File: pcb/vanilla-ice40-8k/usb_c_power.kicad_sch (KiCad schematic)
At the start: 25 parts, among them J5 Conn_01x02_Pin, U5 TPS563252DRLR, U6 TPS563252DRLR

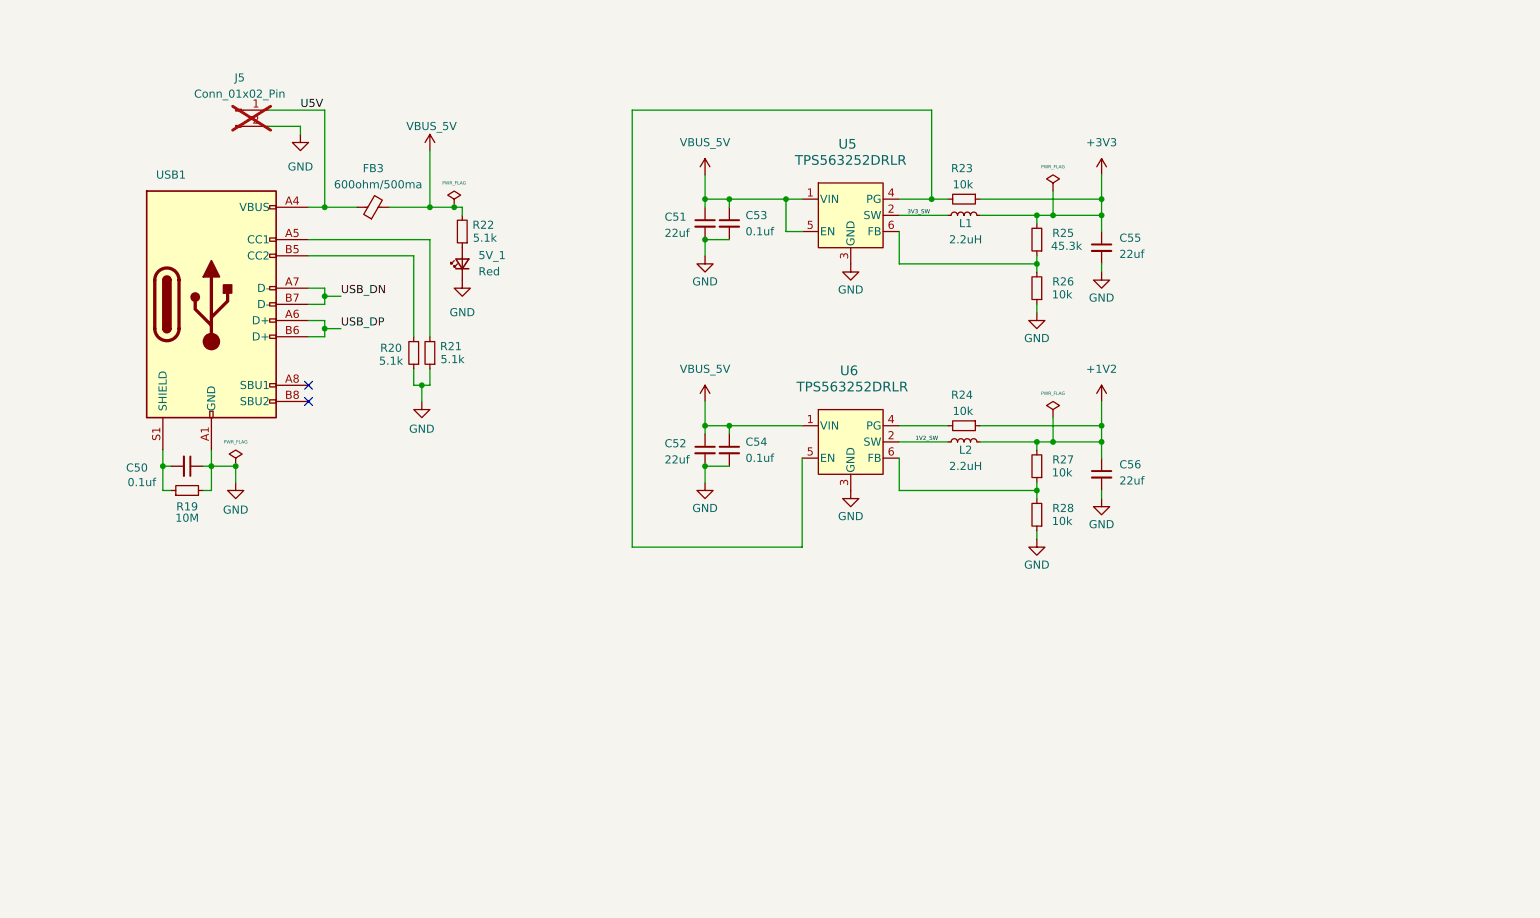
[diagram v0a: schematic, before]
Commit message: [pcb][hx8k] redid components with vip
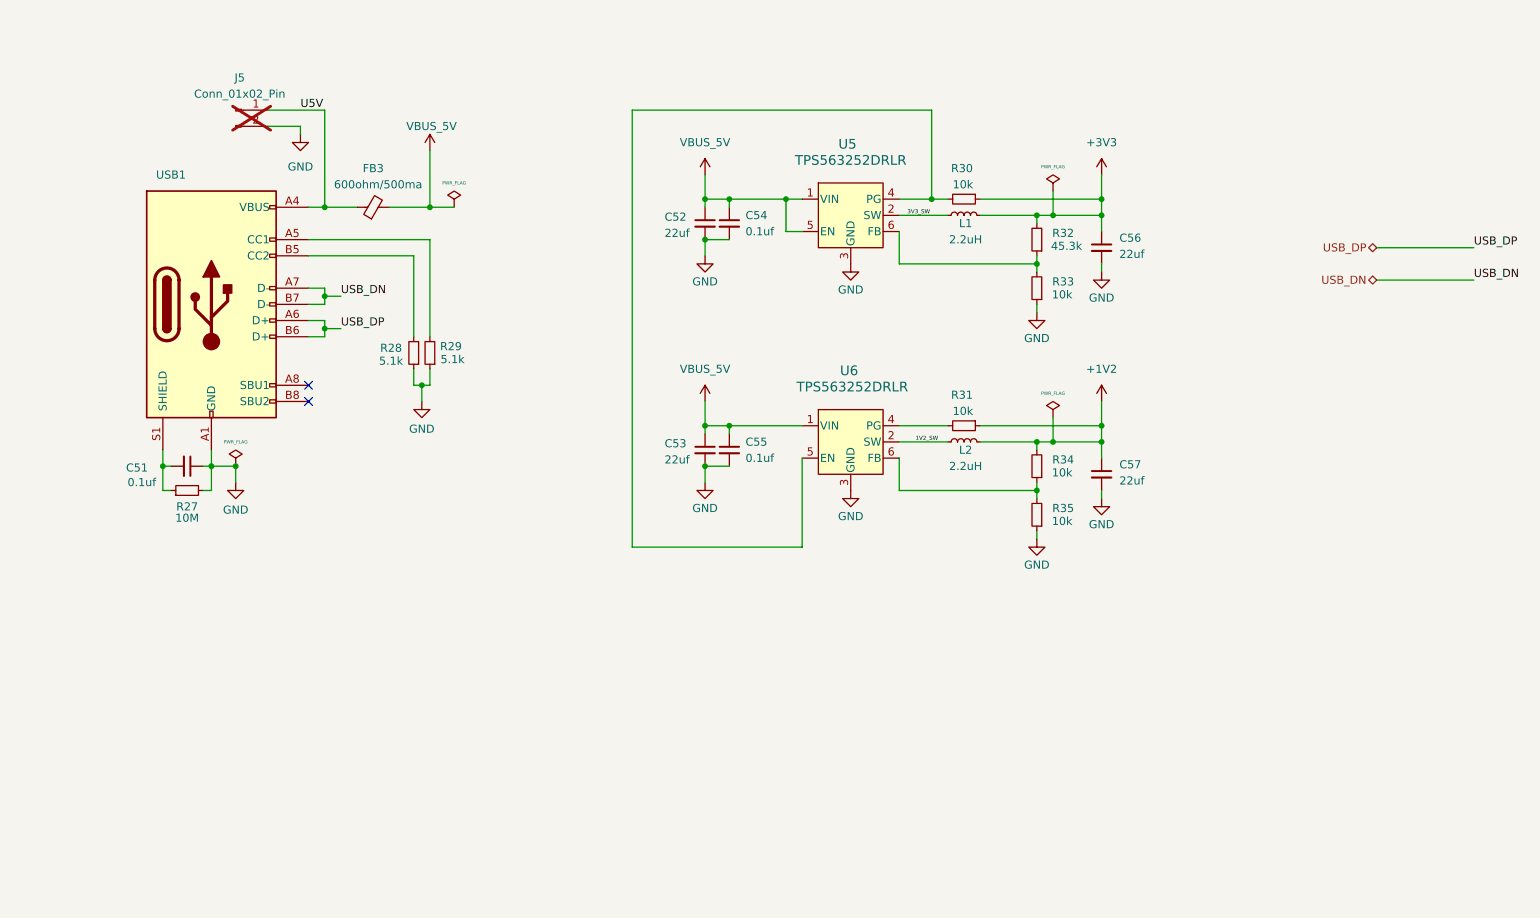
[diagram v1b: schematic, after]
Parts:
- removed 5V_1: Red, Diode_SMD:D_0603_1608Metric, symbol Device:LED_Small
- removed R22: 5.1k, Resistor_SMD:R_0603_1608Metric, symbol Device:R_Small
- renumbered C50 to C51, C51 to C52, C52 to C53, C53 to C54, C54 to C55, C55 to C56, C56 to C57, R19 to R27, R20 to R28, R21 to R29, R23 to R30, R24 to R31, R25 to R32, R26 to R33, R27 to R34, R28 to R35

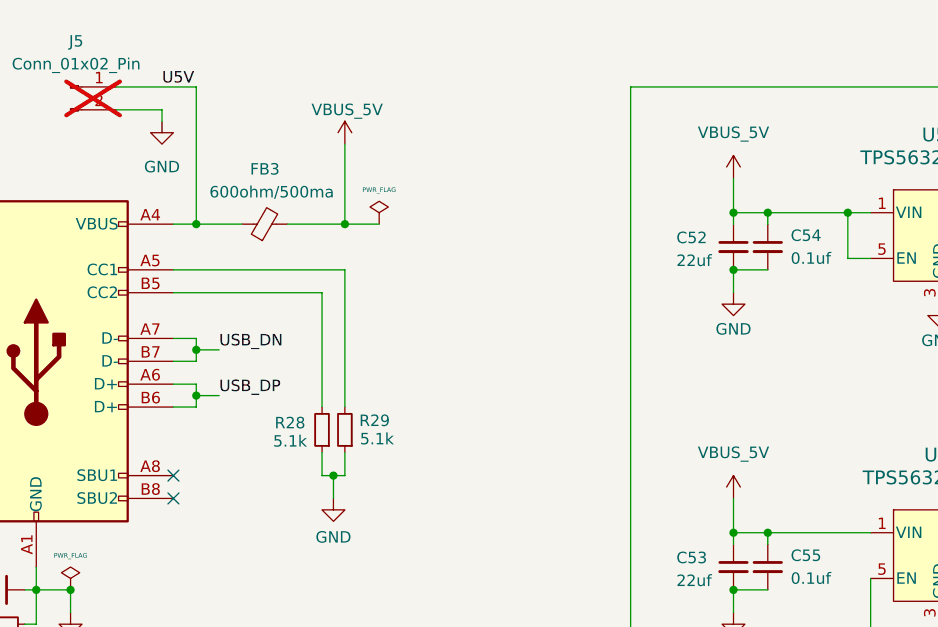
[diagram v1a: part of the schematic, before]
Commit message: [pcb][hx8k] incoming power cleanup
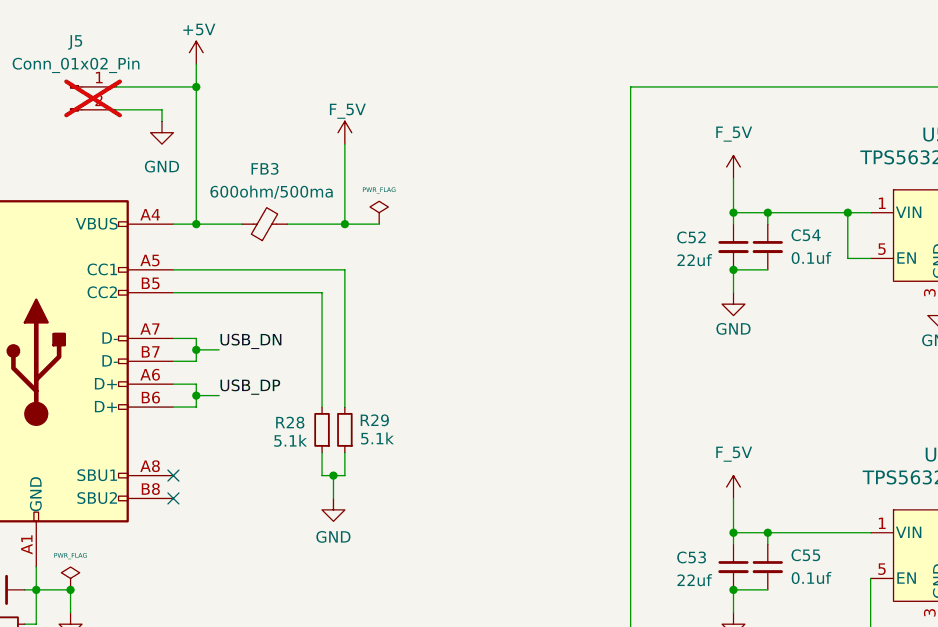
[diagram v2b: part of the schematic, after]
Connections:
- net U5V renamed +5V
- net VBUS_5V renamed F_5V
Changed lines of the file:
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@@
 	)
 	(junction
+		(at 73.66 39.37)
+		(diameter 0)
+		(color 0 0 0 0)
+	)
+	(junction
 		(at 88.9 82.55)
 		(diameter 0)
@@
 	(wire
 		(pts
+			(xy 73.66 36.83) (xy 73.66 39.37)
+		)
+		(stroke
+			(width 0)
+			(type default)
+		)
+	)
+	(wire
+		(pts
 			(xy 133.35 53.34) (xy 133.35 54.61)
 		)
@@
 		)
 	)
-	(label "U5V"
-		(at 69.85 39.37 0)
-		(fields_autoplaced yes)
-		(effects
-			(font
-				(size 1.27 1.27)
-			)
-			(justify left bottom)
-		)
-	)
 	(label "USB_DP"
 		(at 254 60.96 0)
@@
 			)
 		)
-		(property "Value" "VBUS_5V"
+		(property "Value" "F_5V"
 			(at 133.35 80.01 0)
 			(effects
@@
 	)
 	(symbol
+		(lib_id "power:VBUS")
+		(at 73.66 36.83 0)
+		(unit 1)
+		(exclude_from_sim no)
+		(in_bom yes)
+		(on_board yes)
+		(dnp no)
+		(property "Reference" "#PWR078"
+			(at 73.66 40.64 0)
+			(effects
+				(font
+					(size 1.27 1.27)
+				)
+				(hide yes)
+			)
+		)
+		(property "Value" "+5V"
+			(at 73.914 33.02 0)
+			(effects
+				(font
+					(size 1.27 1.27)
+				)
+			)
+		)
+		(property "Footprint" ""
+			(at 73.66 36.83 0)
+			(effects
+				(font
+					(size 1.27 1.27)
+				)
+				(hide yes)
+			)
+		)
+		(property "Datasheet" ""
+			(at 73.66 36.83 0)
+			(effects
+				(font
+					(size 1.27 1.27)
+				)
+				(hide yes)
+			)
+		)
+		(property "Description" "Power symbol creates a global label with name \"VBUS\""
+			(at 73.66 36.83 0)
+			(effects
+				(font
+					(size 1.27 1.27)
+				)
+				(hide yes)
+			)
+		)
+		(pin "1"
+		)
+		(instances
+			(project "vanilla-ice40-8k"
+				(path "/6fdfbf4b-014a-4077-8dc3-7ce5ecaf5fe5/4c09157d-3537-4cf3-bc9c-21379ec730e4"
+					(reference "#PWR078")
+					(unit 1)
+				)
+			)
+		)
+	)
+	(symbol
 		(lib_id "power:GND")
 		(at 195.58 64.77 0)
@@
 			)
 		)
-		(property "Value" "VBUS_5V"
+		(property "Value" "F_5V"
 			(at 133.35 44.45 0)
 			(effects
@@
 			)
 		)
-		(property "Value" "VBUS_5V"
+		(property "Value" "F_5V"
 			(at 90.424 41.91 0)
 			(effects

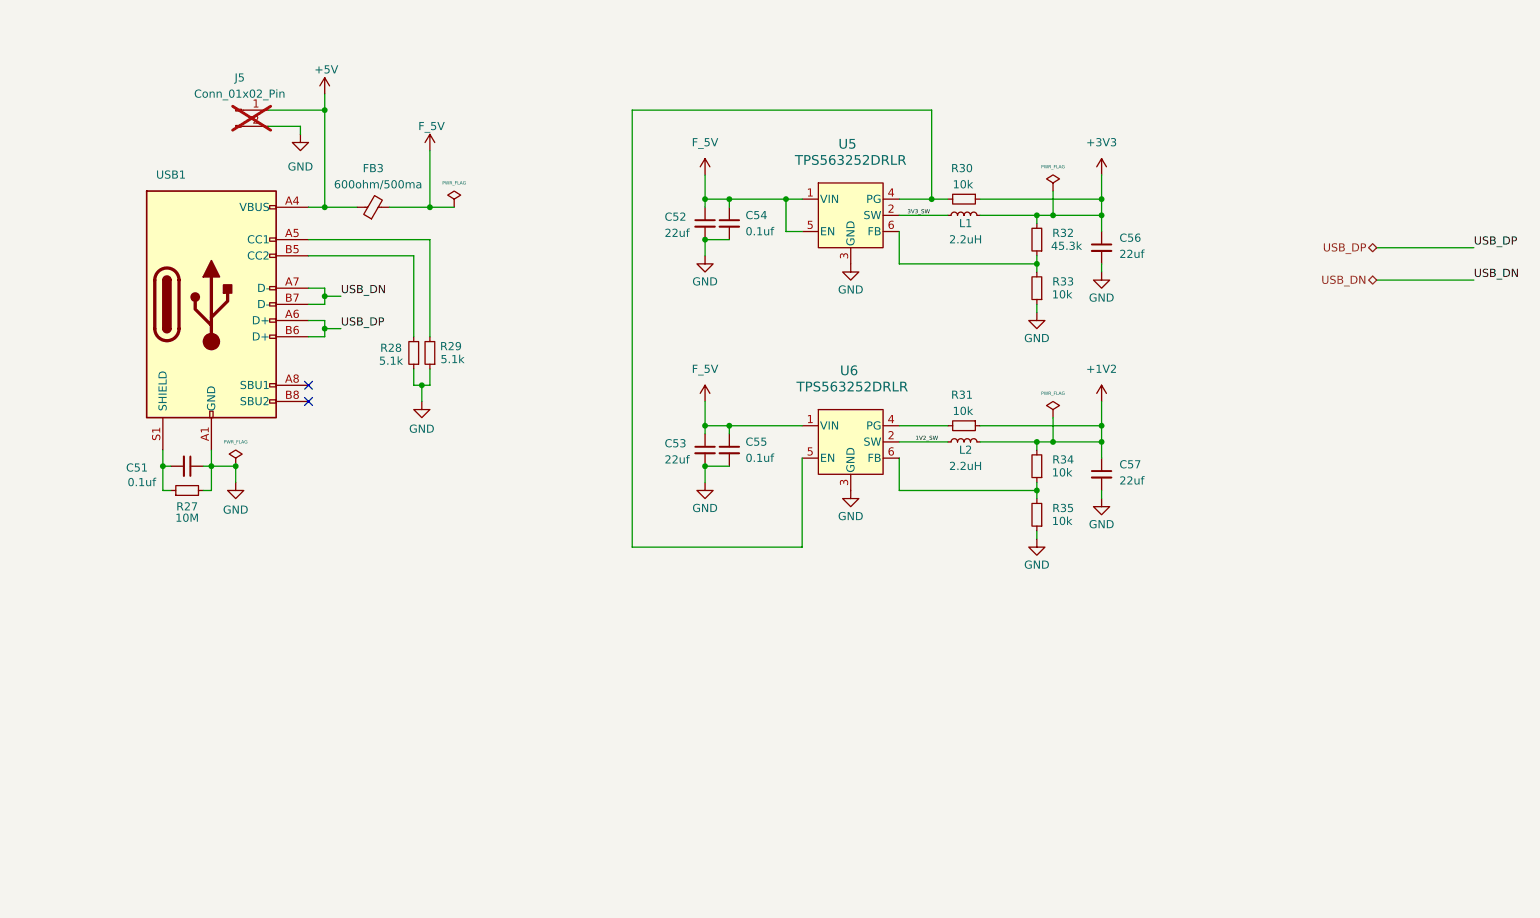
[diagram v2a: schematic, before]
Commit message: [pcb][hx8k] rerouted; all pins done
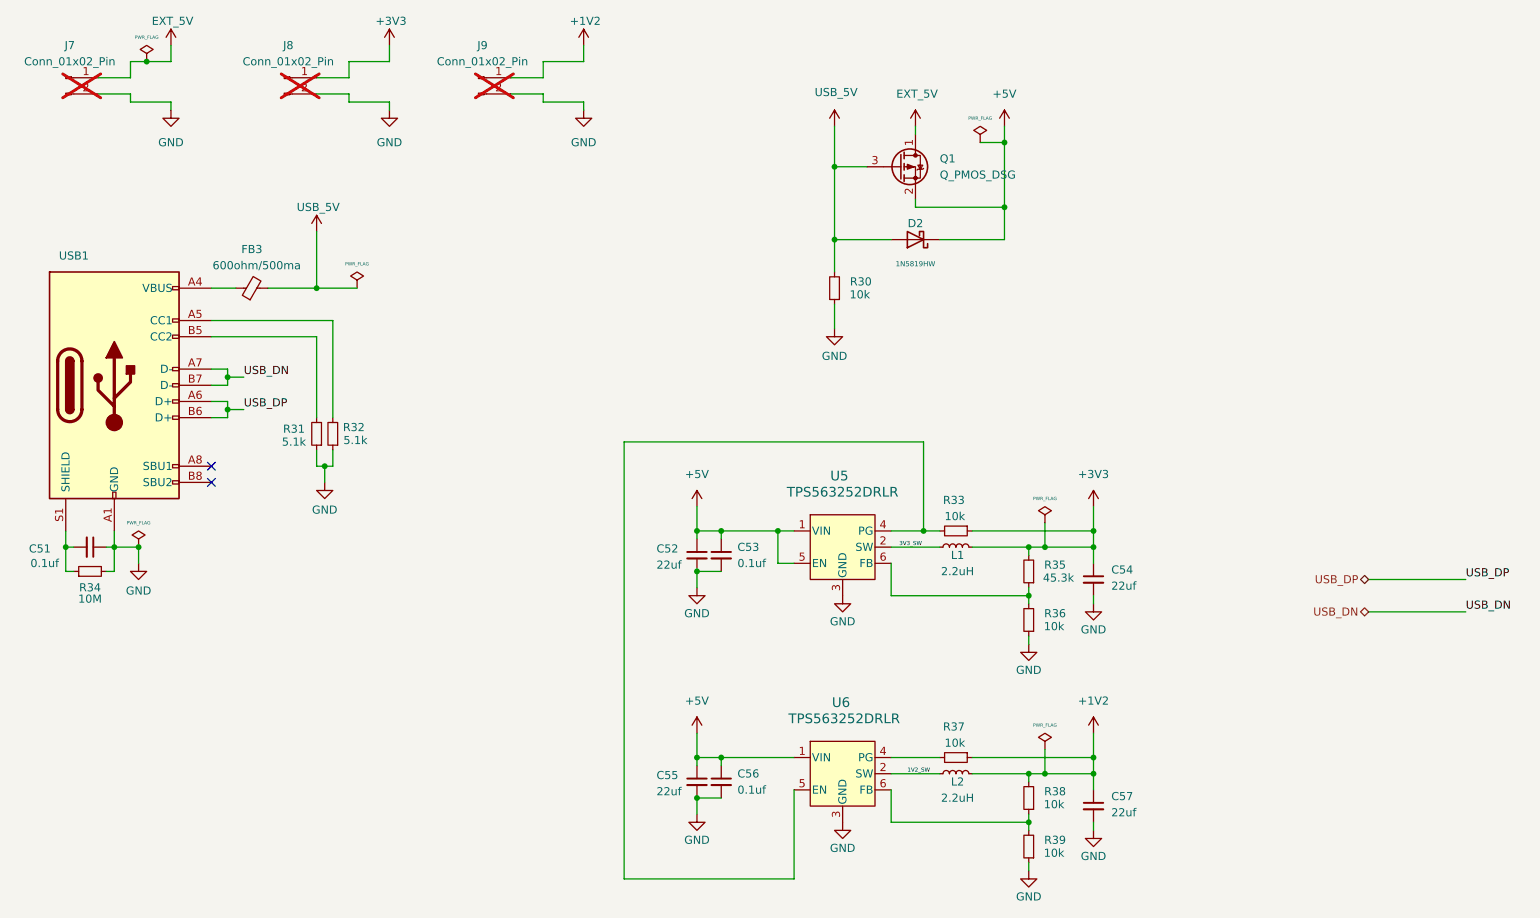
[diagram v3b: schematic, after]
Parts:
- removed J5: Conn_01x02_Pin, Connector_PinHeader_2.54mm:PinHeader_1x02_P2.54mm_Vertical, symbol Connector:Conn_01x02_Pin
- added D2: 1N5819HW, Diode_SMD:D_SOD-123, symbol Diode:1N5819
- added J7, J8, J9: Conn_01x02_Pin, Connector_PinHeader_2.54mm:PinHeader_1x02_P2.54mm_Vertical, symbol Connector:Conn_01x02_Pin
- added Q1: Q_PMOS_DSG, Package_TO_SOT_SMD:SOT-23-3, symbol Device:Q_PMOS_DSG
- added R30: 10k, Resistor_SMD:R_0603_1608Metric, symbol Device:R_Small
- renumbered C54 to C53, C56 to C54, C53 to C55, C55 to C56, R28 to R31, R29 to R32, R30 to R33, R27 to R34, R32 to R35, R33 to R36, R31 to R37, R34 to R38, R35 to R39
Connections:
- net +1V2: now also J9.1 (Pin_1)
- net +3V3: now also J8.1 (Pin_1)
- net +5V: now also C52.1, C53.1, C55.1, C56.1, U5.1 (VIN), U5.5 (EN), U6.1 (VIN), D2.1 (K), Q1.2 (S); no longer FB3.1, USB1.A4 (VBUS), USB1.A9 (VBUS), USB1.B4 (VBUS), USB1.B9 (VBUS)
- net GND: now also J7.2 (Pin_2), J8.2 (Pin_2), J9.2 (Pin_2), R30.1
- removed net F_5V: C52.1, C53.1, C55.1, C56.1, FB3.2, U5.1 (VIN), U5.5 (EN), U6.1 (VIN)
- new net: FB3.1, USB1.A4 (VBUS), USB1.A9 (VBUS), USB1.B4 (VBUS), USB1.B9 (VBUS)
- new net EXT_5V: J7.1 (Pin_1), Q1.1 (D)
- new net USB_5V: D2.2 (A), FB3.2, Q1.3 (G), R30.2
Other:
- moved on the sheet: C51, C52, C53, C54, C55, C56, C57, FB3, L1, L2, R31, R32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

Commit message: [pcb][hx8k] finalize for production
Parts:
- D2: Digi-Key Part Number (none) -> 1N5819HW-FDICT-ND; LCSC Part # (none) -> C82544
- J7, J8, J9: Digi-Key Part Number (none) -> DNP; LCSC Part # (none) -> DNP
- Q1: value Q_PMOS_DSG -> 1N5819HW; Digi-Key Part Number (none) -> 1N5819HW-FDICT-ND; LCSC Part # (none) -> C82544
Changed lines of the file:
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@@
 			)
 		)
+		(property "Digi-Key Part Number" "1N5819HW-FDICT-ND"
+			(at 166.37 59.69 0)
+			(effects
+				(font
+					(size 1.27 1.27)
+				)
+				(hide yes)
+			)
+		)
+		(property "LCSC Part #" "C82544"
+			(at 166.37 59.69 0)
+			(effects
+				(font
+					(size 1.27 1.27)
+				)
+				(hide yes)
+			)
+		)
 		(pin "1"
 		)
@@
 			)
 		)
-		(property "Digi-Key Part Number" ""
+		(property "Digi-Key Part Number" "DNP"
+			(at 33.02 34.29 0)
+			(effects
+				(font
+					(size 1.27 1.27)
+				)
+				(hide yes)
+			)
+		)
+		(property "LCSC Part #" "DNP"
 			(at 33.02 34.29 0)
 			(effects
@@
 			)
 		)
-		(property "Value" "Q_PMOS_DSG"
+		(property "Value" "1N5819HW"
 			(at 170.18 49.5299 0)
 			(effects
@@
 			)
 		)
+		(property "Digi-Key Part Number" "1N5819HW-FDICT-ND"
+			(at 163.83 48.26 0)
+			(effects
+				(font
+					(size 1.27 1.27)
+				)
+				(hide yes)
+			)
+		)
+		(property "LCSC Part #" "C82544"
+			(at 163.83 48.26 0)
+			(effects
+				(font
+					(size 1.27 1.27)
+				)
+				(hide yes)
+			)
+		)
 		(pin "3"
 		)
@@
 			)
 		)
-		(property "Digi-Key Part Number" ""
+		(property "Digi-Key Part Number" "DNP"
+			(at 67.31 34.29 0)
+			(effects
+				(font
+					(size 1.27 1.27)
+				)
+				(hide yes)
+			)
+		)
+		(property "LCSC Part #" "DNP"
 			(at 67.31 34.29 0)
 			(effects
@@
 			)
 		)
-		(property "Digi-Key Part Number" ""
+		(property "Digi-Key Part Number" "DNP"
+			(at 97.79 34.29 0)
+			(effects
+				(font
+					(size 1.27 1.27)
+				)
+				(hide yes)
+			)
+		)
+		(property "LCSC Part #" "DNP"
 			(at 97.79 34.29 0)
 			(effects

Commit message: [pcb][hx8k] submitted to jlcpcb
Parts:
- Q1: value 1N5819HW -> DMG2305UX-13; Digi-Key Part Number 1N5819HW-FDICT-ND -> DMG2305UX-13DICT-ND; LCSC Part # C82544 -> C144153
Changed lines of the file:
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@@
 			)
 		)
-		(property "Datasheet" "http://www.vishay.com/docs/88525/1n5817.pdf"
+		(property "Datasheet" ""
 			(at 166.37 59.69 0)
 			(effects
@@
 			)
 		)
-		(property "Value" "1N5819HW"
+		(property "Value" "DMG2305UX-13"
 			(at 170.18 49.5299 0)
 			(effects
@@
 			)
 		)
-		(property "Datasheet" "~"
+		(property "Datasheet" ""
 			(at 163.83 48.26 0)
 			(effects
@@
 			)
 		)
-		(property "Digi-Key Part Number" "1N5819HW-FDICT-ND"
+		(property "Digi-Key Part Number" "DMG2305UX-13DICT-ND"
 			(at 163.83 48.26 0)
 			(effects
@@
 			)
 		)
-		(property "LCSC Part #" "C82544"
+		(property "LCSC Part #" "C144153"
 			(at 163.83 48.26 0)
 			(effects

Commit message: [hx8k][pcb] correct fb rating to 1.5A
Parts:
- FB3: value 600ohm/500ma -> 600ohm/1.5A
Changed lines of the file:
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@@
 			)
 		)
-		(property "Value" "600ohm/500ma"
+		(property "Value" "600ohm/1.5A"
 			(at 62.992 63.754 90)
 			(effects

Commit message: [hx8k][pcb] place and route stackable connector on left
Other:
- title: (none) -> Vanilia Ice HX8K
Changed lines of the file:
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@@
 	(generator_version "8.0")
 	(paper "A4")
+	(title_block
+		(title "Vanilia Ice HX8K")
+		(rev "1.5.0")
+	)
 	(junction
 		(at 180.34 44.45)
